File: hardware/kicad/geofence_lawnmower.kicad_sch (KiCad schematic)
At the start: 20 parts, among them J1 Raspberry Pi 5 (J8 40-pin GPI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, U1 NEO-M8N GPS, U2 HC-SR04 (Front)

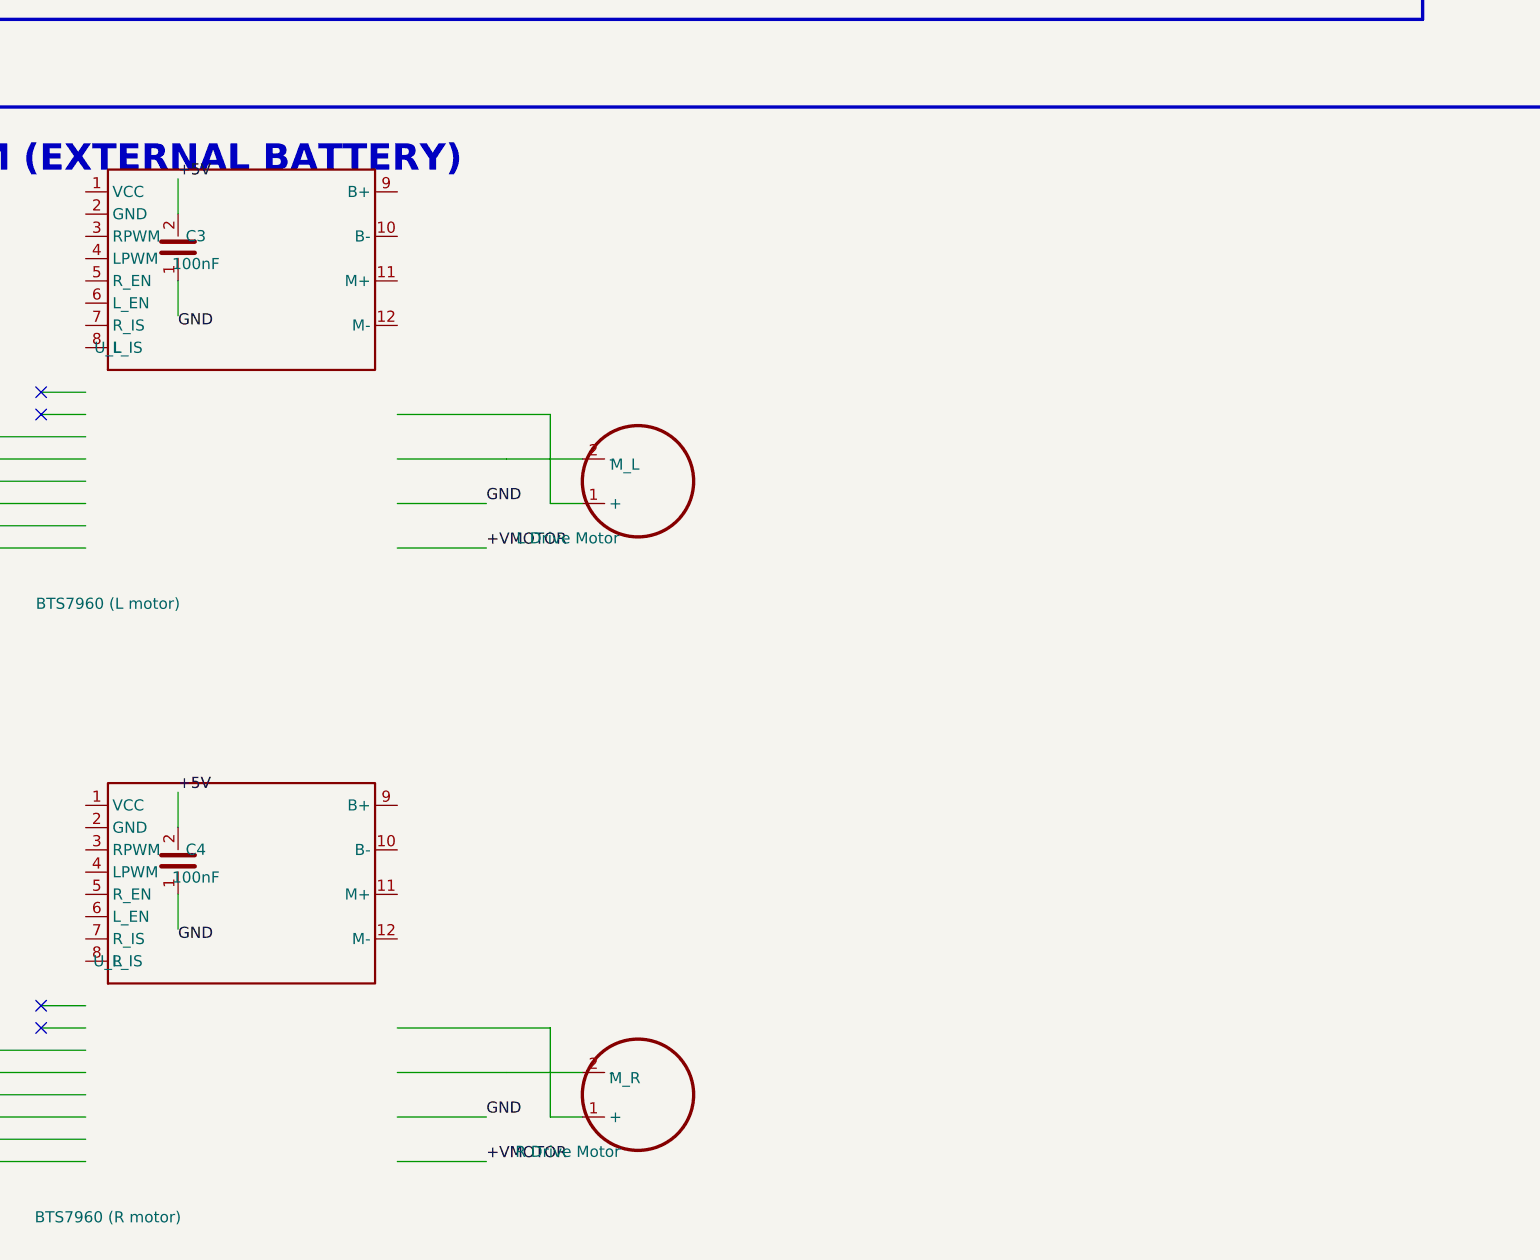
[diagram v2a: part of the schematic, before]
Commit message: fix: Move BTS7960 decoupling caps clear of the driver's pin rows
The previous placement (just above the driver body) ended up colliding
with the driver's own pin rows once the row-reversal fix changed where
they render. Moved C3/C4 well clear into open space to the right instead
of trying to track the driver's rendered extent.

Co-Authored-By: Claude Sonnet 5 <noreply@anthropic.com>
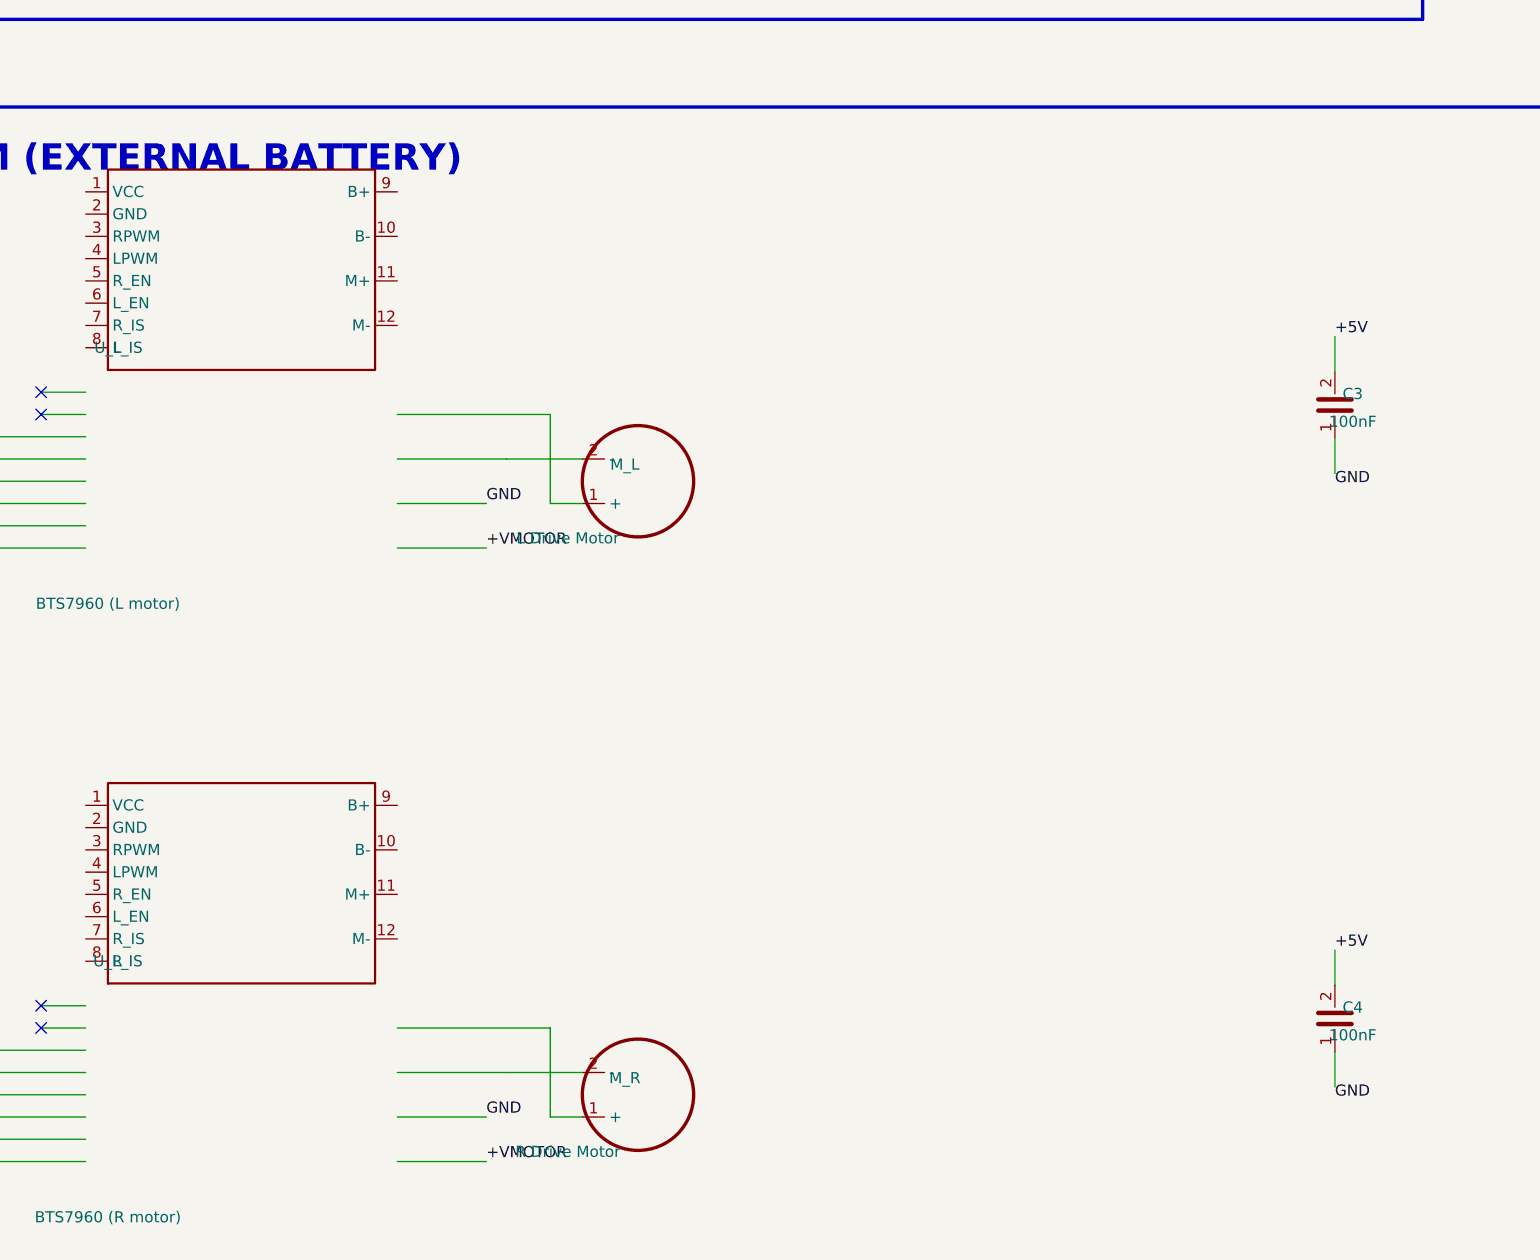
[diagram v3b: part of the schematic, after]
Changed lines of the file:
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@@
   (instances
     (project "geofence_lawnmower"
-      (path "/d6390fb0-74a3-4fe7-be88-cf910882c09e" (reference "J1") (unit 1))
+      (path "/cf86c55a-da09-4998-83a1-311fe32a58b6" (reference "J1") (unit 1))
     )
   )
@@
   (instances
     (project "geofence_lawnmower"
-      (path "/d6390fb0-74a3-4fe7-be88-cf910882c09e" (reference "U1") (unit 1))
+      (path "/cf86c55a-da09-4998-83a1-311fe32a58b6" (reference "U1") (unit 1))
     )
   )
@@
   (instances
     (project "geofence_lawnmower"
-      (path "/d6390fb0-74a3-4fe7-be88-cf910882c09e" (reference "C1") (unit 1))
+      (path "/cf86c55a-da09-4998-83a1-311fe32a58b6" (reference "C1") (unit 1))
     )
   )
@@
   (instances
     (project "geofence_lawnmower"
-      (path "/d6390fb0-74a3-4fe7-be88-cf910882c09e" (reference "BZ1") (unit 1))
+      (path "/cf86c55a-da09-4998-83a1-311fe32a58b6" (reference "BZ1") (unit 1))
     )
   )
@@
   (instances
     (project "geofence_lawnmower"
-      (path "/d6390fb0-74a3-4fe7-be88-cf910882c09e" (reference "R1") (unit 1))
+      (path "/cf86c55a-da09-4998-83a1-311fe32a58b6" (reference "R1") (unit 1))
     )
   )
@@
   (instances
     (project "geofence_lawnmower"
-      (path "/d6390fb0-74a3-4fe7-be88-cf910882c09e" (reference "D1") (unit 1))
+      (path "/cf86c55a-da09-4998-83a1-311fe32a58b6" (reference "D1") (unit 1))
     )
   )
@@
   (instances
     (project "geofence_lawnmower"
-      (path "/d6390fb0-74a3-4fe7-be88-cf910882c09e" (reference "R2") (unit 1))
+      (path "/cf86c55a-da09-4998-83a1-311fe32a58b6" (reference "R2") (unit 1))
     )
   )
@@
   (instances
     (project "geofence_lawnmower"
-      (path "/d6390fb0-74a3-4fe7-be88-cf910882c09e" (reference "D2") (unit 1))
+      (path "/cf86c55a-da09-4998-83a1-311fe32a58b6" (reference "D2") (unit 1))
     )
   )
@@
   (instances
     (project "geofence_lawnmower"
-      (path "/d6390fb0-74a3-4fe7-be88-cf910882c09e" (reference "U2") (unit 1))
+      (path "/cf86c55a-da09-4998-83a1-311fe32a58b6" (reference "U2") (unit 1))
     )
   )
@@
   (instances
     (project "geofence_lawnmower"
-      (path "/d6390fb0-74a3-4fe7-be88-cf910882c09e" (reference "R3") (unit 1))
+      (path "/cf86c55a-da09-4998-83a1-311fe32a58b6" (reference "R3") (unit 1))
     )
   )
@@
   (instances
     (project "geofence_lawnmower"
-      (path "/d6390fb0-74a3-4fe7-be88-cf910882c09e" (reference "R4") (unit 1))
+      (path "/cf86c55a-da09-4998-83a1-311fe32a58b6" (reference "R4") (unit 1))
     )
   )
@@
   (instances
     (project "geofence_lawnmower"
-      (path "/d6390fb0-74a3-4fe7-be88-cf910882c09e" (reference "C2") (unit 1))
+      (path "/cf86c55a-da09-4998-83a1-311fe32a58b6" (reference "C2") (unit 1))
     )
   )
@@
   (instances
     (project "geofence_lawnmower"
-      (path "/d6390fb0-74a3-4fe7-be88-cf910882c09e" (reference "U_L") (unit 1))
+      (path "/cf86c55a-da09-4998-83a1-311fe32a58b6" (reference "U_L") (unit 1))
     )
   )
@@
   (instances
     (project "geofence_lawnmower"
-      (path "/d6390fb0-74a3-4fe7-be88-cf910882c09e" (reference "M_L") (unit 1))
+      (path "/cf86c55a-da09-4998-83a1-311fe32a58b6" (reference "M_L") (unit 1))
     )
   )
@@
 (wire (pts (xy 170.48 280.08) (xy 170.48 290.24)) (stroke (width 0) (type default)))
 (wire (pts (xy 170.48 290.24) (xy 174.13 290.24)) (stroke (width 0) (type default)))
-(symbol (lib_id "GEO:C") (at 128 261 0) (unit 1)
-  (exclude_from_sim no) (in_bom yes) (on_board yes) (dnp no)
-  (property "Reference" "C3" (at 130.032 259.73 0) (effects (font (size 1.27 1.27))))
-  (property "Value" "100nF" (at 130.032 262.905 0) (effects (font (size 1.27 1.27))))
-  (property "Footprint" "" (at 128 261 0) (effects (font (size 1.27 1.27)) hide))
-  (pin "1")
-(pin "2")
-  (instances
-    (project "geofence_lawnmower"
-      (path "/d6390fb0-74a3-4fe7-be88-cf910882c09e" (reference "C3") (unit 1))
-    )
-  )
-)
-(wire (pts (xy 128 257.19) (xy 128 253.19)) (stroke (width 0) (type default)))
-(label "+5V" (at 128 253.19 0) (effects (font (size 1.27 1.27)) (justify left bottom)))
-(wire (pts (xy 128 264.81) (xy 128 268.81)) (stroke (width 0) (type default)))
-(label "GND" (at 128 268.81 0) (effects (font (size 1.27 1.27)) (justify left top)))
+(symbol (lib_id "GEO:C") (at 260 279 0) (unit 1)
+  (exclude_from_sim no) (in_bom yes) (on_board yes) (dnp no)
+  (property "Reference" "C3" (at 262.032 277.73 0) (effects (font (size 1.27 1.27))))
+  (property "Value" "100nF" (at 262.032 280.905 0) (effects (font (size 1.27 1.27))))
+  (property "Footprint" "" (at 260 279 0) (effects (font (size 1.27 1.27)) hide))
+  (pin "1")
+(pin "2")
+  (instances
+    (project "geofence_lawnmower"
+      (path "/cf86c55a-da09-4998-83a1-311fe32a58b6" (reference "C3") (unit 1))
+    )
+  )
+)
+(wire (pts (xy 260 275.19) (xy 260 271.19)) (stroke (width 0) (type default)))
+(label "+5V" (at 260 271.19 0) (effects (font (size 1.27 1.27)) (justify left bottom)))
+(wire (pts (xy 260 282.81) (xy 260 286.81)) (stroke (width 0) (type default)))
+(label "GND" (at 260 286.81 0) (effects (font (size 1.27 1.27)) (justify left top)))
 (symbol (lib_id "GEO:BTS7960") (at 120 345 0) (unit 1)
   (exclude_from_sim no) (in_bom yes) (on_board yes) (dnp no)
@@
   (instances
     (project "geofence_lawnmower"
-      (path "/d6390fb0-74a3-4fe7-be88-cf910882c09e" (reference "U_R") (unit 1))
+      (path "/cf86c55a-da09-4998-83a1-311fe32a58b6" (reference "U_R") (unit 1))
     )
   )
@@
   (instances
     (project "geofence_lawnmower"
-      (path "/d6390fb0-74a3-4fe7-be88-cf910882c09e" (reference "M_R") (unit 1))
+      (path "/cf86c55a-da09-4998-83a1-311fe32a58b6" (reference "M_R") (unit 1))
     )
   )
@@
 (wire (pts (xy 170.48 350.08) (xy 170.48 360.24)) (stroke (width 0) (type default)))
 (wire (pts (xy 170.48 360.24) (xy 174.13 360.24)) (stroke (width 0) (type default)))
-(symbol (lib_id "GEO:C") (at 128 331 0) (unit 1)
-  (exclude_from_sim no) (in_bom yes) (on_board yes) (dnp no)
-  (property "Reference" "C4" (at 130.032 329.73 0) (effects (font (size 1.27 1.27))))
-  (property "Value" "100nF" (at 130.032 332.905 0) (effects (font (size 1.27 1.27))))
-  (property "Footprint" "" (at 128 331 0) (effects (font (size 1.27 1.27)) hide))
-  (pin "1")
-(pin "2")
-  (instances
-    (project "geofence_lawnmower"
-      (path "/d6390fb0-74a3-4fe7-be88-cf910882c09e" (reference "C4") (unit 1))
-    )
-  )
-)
-(wire (pts (xy 128 327.19) (xy 128 323.19)) (stroke (width 0) (type default)))
-(label "+5V" (at 128 323.19 0) (effects (font (size 1.27 1.27)) (justify left bottom)))
-(wire (pts (xy 128 334.81) (xy 128 338.81)) (stroke (width 0) (type default)))
-(label "GND" (at 128 338.81 0) (effects (font (size 1.27 1.27)) (justify left top)))
+(symbol (lib_id "GEO:C") (at 260 349 0) (unit 1)
+  (exclude_from_sim no) (in_bom yes) (on_board yes) (dnp no)
+  (property "Reference" "C4" (at 262.032 347.73 0) (effects (font (size 1.27 1.27))))
+  (property "Value" "100nF" (at 262.032 350.905 0) (effects (font (size 1.27 1.27))))
+  (property "Footprint" "" (at 260 349 0) (effects (font (size 1.27 1.27)) hide))
+  (pin "1")
+(pin "2")
+  (instances
+    (project "geofence_lawnmower"
+      (path "/cf86c55a-da09-4998-83a1-311fe32a58b6" (reference "C4") (unit 1))
+    )
+  )
+)
+(wire (pts (xy 260 345.19) (xy 260 341.19)) (stroke (width 0) (type default)))
+(label "+5V" (at 260 341.19 0) (effects (font (size 1.27 1.27)) (justify left bottom)))
+(wire (pts (xy 260 352.81) (xy 260 356.81)) (stroke (width 0) (type default)))
+(label "GND" (at 260 356.81 0) (effects (font (size 1.27 1.27)) (justify left top)))
 (symbol (lib_id "GEO:BATTERY_PACK") (at 490 325 0) (unit 1)
   (exclude_from_sim no) (in_bom yes) (on_board yes) (dnp no)
@@
   (instances
     (project "geofence_lawnmower"
-      (path "/d6390fb0-74a3-4fe7-be88-cf910882c09e" (reference "BT1") (unit 1))
+      (path "/cf86c55a-da09-4998-83a1-311fe32a58b6" (reference "BT1") (unit 1))
     )
   )
@@
   (instances
     (project "geofence_lawnmower"
-      (path "/d6390fb0-74a3-4fe7-be88-cf910882c09e" (reference "F1") (unit 1))
-    )
-  )
+      (path "/cf86c55a-da09-4998-83a1-311fe32a58b6" (reference "F1") (unit 1))
+    )
+  )
